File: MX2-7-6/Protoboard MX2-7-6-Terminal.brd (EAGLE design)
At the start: 54.4 x 59.2 mm, 293 parts

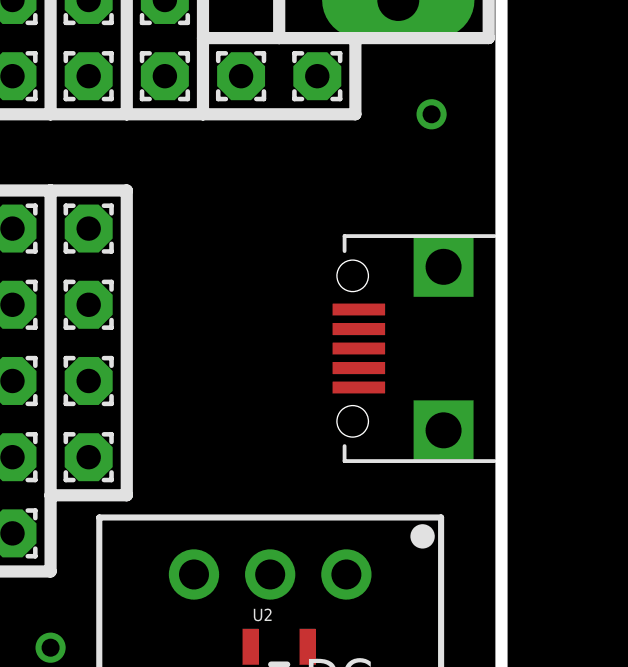
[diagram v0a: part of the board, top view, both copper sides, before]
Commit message: Change usb connector
Change to correct usb connecter and moved esp8266 bit more onto the
board.
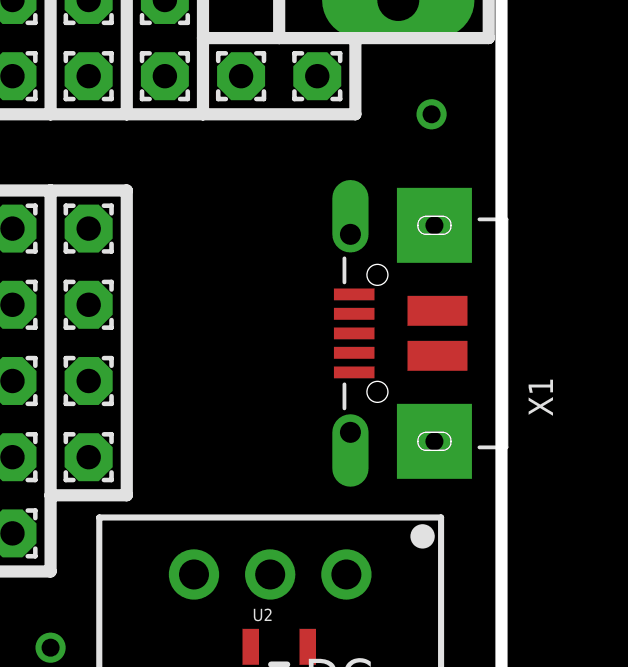
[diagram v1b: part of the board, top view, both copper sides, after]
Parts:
- removed JP1: USB-RECEPTABLE, daspilker:FCI-10103594-0001LF
- added X1: (no value), microbuilder:4UCONN_20329
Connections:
- net GND: now also X1.BASE@1, X1.BASE@2, X1.GND, X1.SPRT@1, X1.SPRT@2, X1.SPRT@3, X1.SPRT@4; no longer JP1.5
- net VCC: now also X1.VBUS; no longer JP1.1
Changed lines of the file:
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@@
 <attribute name="VALUE" x="33.02" y="55.21" size="0.0254" layer="27"/>
 </element>
-<element name="JP1" library="daspilker" package="FCI-10103594-0001LF" value="USB-RECEPTABLE" x="54.17" y="23.94" smashed="yes" rot="R90"/>
 <element name="U2" library="SparkFun-PowerIC" package="SOT23-5" value="" x="46.99" y="12.7">
 <attribute name="PROD_ID" value="VREG-00822" x="46.99" y="12.7" size="1.778" layer="27" display="off"/>
@@
 <attribute name="VALUE" x="44.45" y="40.005" size="1.27" layer="27"/>
 </element>
+<element name="X1" library="microbuilder" package="4UCONN_20329" value="" x="50.265" y="24.4475" rot="R90"/>
 </elements>
 <signals>
@@
 <contactref element="PAD33" pad="1"/>
 <contactref element="PAD36" pad="1"/>
-<contactref element="JP1" pad="5"/>
 <contactref element="U2" pad="2"/>
-<wire x1="40.64" y1="54.61" x2="43.18" y2="54.61" width="0" layer="19" extent="1-1"/>
-<wire x1="38.1" y1="54.61" x2="40.64" y2="54.61" width="0" layer="19" extent="1-1"/>
-<wire x1="35.56" y1="54.61" x2="38.1" y2="54.61" width="0" layer="19" extent="1-1"/>
-<wire x1="33.02" y1="54.61" x2="35.56" y2="54.61" width="0" layer="19" extent="1-1"/>
-<wire x1="30.48" y1="54.61" x2="33.02" y2="54.61" width="0" layer="19" extent="1-1"/>
-<wire x1="27.94" y1="54.61" x2="30.48" y2="54.61" width="0" layer="19" extent="1-1"/>
-<wire x1="25.4" y1="54.61" x2="27.94" y2="54.61" width="0" layer="19" extent="1-1"/>
-<wire x1="22.86" y1="54.61" x2="25.4" y2="54.61" width="0" layer="19" extent="1-1"/>
-<wire x1="20.32" y1="54.61" x2="22.86" y2="54.61" width="0" layer="19" extent="1-1"/>
-<wire x1="17.78" y1="54.61" x2="20.32" y2="54.61" width="0" layer="19" extent="1-1"/>
-<wire x1="15.24" y1="54.61" x2="17.78" y2="54.61" width="0" layer="19" extent="1-1"/>
-<wire x1="12.7" y1="54.61" x2="15.24" y2="54.61" width="0" layer="19" extent="1-1"/>
-<wire x1="10.16" y1="54.61" x2="12.7" y2="54.61" width="0" layer="19" extent="1-1"/>
-<wire x1="7.62" y1="54.61" x2="10.16" y2="54.61" width="0" layer="19" extent="1-1"/>
-<wire x1="5.08" y1="54.61" x2="7.62" y2="54.61" width="0" layer="19" extent="1-1"/>
-<wire x1="49.645" y1="25.24" x2="43.18" y2="54.61" width="0" layer="19" extent="1-1"/>
-<wire x1="46.69" y1="16.41" x2="49.645" y2="25.24" width="0" layer="19" extent="1-1"/>
-<wire x1="46.99" y1="11.3999" x2="46.69" y2="16.41" width="0" layer="19" extent="1-1"/>
-<wire x1="48.26" y1="5.08" x2="46.99" y2="11.3999" width="0" layer="19" extent="1-1"/>
-<wire x1="50.8" y1="5.08" x2="48.26" y2="5.08" width="0" layer="19" extent="1-1"/>
-<wire x1="45.72" y1="5.08" x2="48.26" y2="5.08" width="0" layer="19" extent="1-1"/>
-<wire x1="43.18" y1="5.08" x2="45.72" y2="5.08" width="0" layer="19" extent="1-1"/>
-<wire x1="40.64" y1="5.08" x2="43.18" y2="5.08" width="0" layer="19" extent="1-1"/>
-<wire x1="38.1" y1="5.08" x2="40.64" y2="5.08" width="0" layer="19" extent="1-1"/>
-<wire x1="35.56" y1="5.08" x2="38.1" y2="5.08" width="0" layer="19" extent="1-1"/>
-<wire x1="33.02" y1="5.08" x2="35.56" y2="5.08" width="0" layer="19" extent="1-1"/>
-<wire x1="30.48" y1="5.08" x2="33.02" y2="5.08" width="0" layer="19" extent="1-1"/>
-<wire x1="27.94" y1="5.08" x2="30.48" y2="5.08" width="0" layer="19" extent="1-1"/>
-<wire x1="25.4" y1="5.08" x2="27.94" y2="5.08" width="0" layer="19" extent="1-1"/>
-<wire x1="22.86" y1="5.08" x2="25.4" y2="5.08" width="0" layer="19" extent="1-1"/>
-<wire x1="20.32" y1="5.08" x2="22.86" y2="5.08" width="0" layer="19" extent="1-1"/>
-<wire x1="17.78" y1="5.08" x2="20.32" y2="5.08" width="0" layer="19" extent="1-1"/>
-<wire x1="15.24" y1="5.08" x2="17.78" y2="5.08" width="0" layer="19" extent="1-1"/>
-<wire x1="12.7" y1="5.08" x2="15.24" y2="5.08" width="0" layer="19" extent="1-1"/>
-<wire x1="10.16" y1="5.08" x2="12.7" y2="5.08" width="0" layer="19" extent="1-1"/>
-<wire x1="7.62" y1="5.08" x2="10.16" y2="5.08" width="0" layer="19" extent="1-1"/>
-<wire x1="5.08" y1="5.08" x2="7.62" y2="5.08" width="0" layer="19" extent="1-1"/>
+<contactref element="X1" pad="SPRT@4"/>
+<contactref element="X1" pad="BASE@2"/>
+<contactref element="X1" pad="SPRT@3"/>
+<contactref element="X1" pad="GND"/>
+<contactref element="X1" pad="SPRT@2"/>
+<contactref element="X1" pad="BASE@1"/>
+<contactref element="X1" pad="SPRT@1"/>
 </signal>
 <signal name="VCC">
 <contactref element="DC" pad="1"/>
-<contactref element="JP1" pad="1"/>
 <contactref element="U2" pad="3"/>
 <contactref element="U2" pad="1"/>
-<wire x1="49.23" y1="16.41" x2="49.645" y2="22.64" width="0" layer="19" extent="1-1"/>
+<contactref element="X1" pad="VBUS"/>
+<wire x1="49.23" y1="16.41" x2="49.49" y2="23.1475" width="0" layer="19" extent="1-1"/>
 <wire x1="47.94" y1="11.3999" x2="49.23" y2="16.41" width="0" layer="19" extent="1-1"/>
 <wire x1="46.04" y1="11.3999" x2="47.94" y2="11.3999" width="0" layer="19" extent="1-1"/>
@@
 <contactref element="JP6" pad="1"/>
 <contactref element="JP2" pad="P$1"/>
-<wire x1="50.96" y1="50.8" x2="45.72" y2="48.26" width="0" layer="19" extent="1-1"/>
+<wire x1="45.72" y1="48.26" x2="50.96" y2="50.8" width="0" layer="19" extent="1-1"/>
 </signal>
 <signal name="N$4">
 <contactref element="JP3" pad="P$1"/>
 <contactref element="JP7" pad="1"/>
-<wire x1="50.96" y1="43.18" x2="45.72" y2="45.72" width="0" layer="19" extent="1-1"/>
+<wire x1="45.72" y1="45.72" x2="50.96" y2="43.18" width="0" layer="19" extent="1-1"/>
 </signal>
 <signal name="N$5">

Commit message: Update esp component and usb
test
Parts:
- removed JP4: (no value), adafruit:1X1-BIGPOGO
- removed JP6, JP7, JP8: (no value), adafruit:1X01-CLEANBIG
- removed PAD1, PAD100, PAD101, PAD102, PAD103, PAD106, PAD107, PAD108, PAD109, PAD110, PAD111, PAD112, PAD115, PAD116, PAD117, PAD118, PAD119, PAD120, PAD121, PAD124, PAD125, PAD126, PAD127, PAD128, PAD129, PAD130, PAD133, PAD134, PAD135, PAD136, PAD137, PAD138, PAD139, PAD142, PAD143, PAD144, PAD145, PAD146, PAD147, PAD148, PAD151, PAD152, PAD153, PAD154, PAD155, PAD156, PAD157, PAD160, PAD161, PAD162, PAD163, PAD164, PAD165, PAD166, PAD169, PAD170, PAD171, PAD172, PAD173, PAD174, PAD175, PAD178, PAD179, PAD180, PAD181, PAD182, PAD183, PAD184, PAD187, PAD188, PAD189, PAD190, PAD191, PAD192, PAD193, PAD196, PAD197, PAD198, PAD199, PAD2, PAD200, PAD201, PAD202, PAD205, PAD206, PAD207, PAD208, PAD209, PAD210, PAD211, PAD214, PAD215, PAD216, PAD217, PAD218, PAD219, PAD220, PAD260, PAD261, PAD262, PAD263, PAD264, PAD265, PAD266, PAD269, PAD270, PAD271, PAD272, PAD273, PAD274, PAD275, PAD278, PAD279, PAD280, PAD281, PAD282, PAD283, PAD284, PAD287, PAD288, PAD289, PAD290, PAD291, PAD292, PAD293, PAD296, PAD297, PAD298, PAD299, PAD300, PAD301, PAD302, PAD305, PAD306, PAD307, PAD308, PAD309, PAD310, PAD311, PAD314, PAD315, PAD316, PAD317, PAD318, PAD319, PAD320, PAD332, PAD333, PAD334, PAD335, PAD336, PAD337, PAD338, PAD341, PAD342, PAD343, PAD344, PAD345, PAD346, PAD347, PAD350, PAD351, PAD352, PAD353, PAD354, PAD355, PAD356, PAD359, PAD360, PAD361, PAD362, PAD363, PAD364, PAD365, PAD368, PAD369, PAD370, PAD371, PAD372, PAD373, PAD374, PAD377, PAD378, PAD379, PAD380, PAD381, PAD382, PAD383, PAD385, PAD386, PAD387, PAD388, PAD389, PAD391, PAD392, PAD393, PAD394, PAD79, PAD80, PAD81, PAD82, PAD83, PAD84, PAD85, PAD88, PAD89, PAD90, PAD91, PAD92, PAD93, PAD94, PAD97, PAD98, PAD99: (no value), wirepad:1,6/0,8
- added J10, J11, J12, J13, J14, J15, J16, J17, J18, J19, J2, J20, J21, J22, J23, J24, J25, J26, J27, J28, J29, J3, J30, J4, J5, J6, J7, J8, J9: (no value), SparkFun-Connectors:1X07_NO_SILK
- added J31: (no value), SparkFun-Connectors:1X05_NO_SILK
- added J32: (no value), SparkFun-Connectors:1X03_NO_SILK
- added J36, J37, J38: (no value), SparkFun-Connectors:1X01_NO_SILK
- added JP1: (no value), adafruit:1X1-BIGPOGO
- moved JP2 9.53 mm to (51.0, 41.3)
- moved JP3 3.18 mm to (51.0, 46.4)
- moved X1 2.22 mm to (50.3, 26.7)
- moved U2 0.64 mm to (46.4, 12.7), turned to 180 degrees
- moved DC 0.64 mm to (46.7, 17.0)
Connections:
- removed net N$40: PAD377.1, PAD378.1, PAD379.1, PAD380.1, PAD381.1, PAD382.1, PAD383.1
- removed net N$41: PAD385.1, PAD386.1, PAD387.1, PAD388.1, PAD389.1
- new net N$6: J4.1, J4.2, J4.3, J4.4, J4.5, J4.6, J4.7
- net N$1: now also J2.1, J2.2, J2.3, J2.4, J2.5, J2.6, J2.7; no longer PAD391.1, PAD392.1, PAD393.1, PAD394.1
- net N$10: now also J8.1, J8.2, J8.3, J8.4, J8.5, J8.6, J8.7; no longer PAD106.1, PAD107.1, PAD108.1, PAD109.1, PAD110.1, PAD111.1, PAD112.1
- net N$11: now also J9.1, J9.2, J9.3, J9.4, J9.5, J9.6, J9.7; no longer PAD115.1, PAD116.1, PAD117.1, PAD118.1, PAD119.1, PAD120.1, PAD121.1
- net N$12: now also J10.1, J10.2, J10.3, J10.4, J10.5, J10.6, J10.7; no longer PAD124.1, PAD125.1, PAD126.1, PAD127.1, PAD128.1, PAD129.1, PAD130.1
- net N$13: now also J11.1, J11.2, J11.3, J11.4, J11.5, J11.6, J11.7; no longer PAD133.1, PAD134.1, PAD135.1, PAD136.1, PAD137.1, PAD138.1, PAD139.1
- net N$14: now also J12.1, J12.2, J12.3, J12.4, J12.5, J12.6, J12.7; no longer PAD142.1, PAD143.1, PAD144.1, PAD145.1, PAD146.1, PAD147.1, PAD148.1
- net N$15: now also J13.1, J13.2, J13.3, J13.4, J13.5, J13.6, J13.7; no longer PAD151.1, PAD152.1, PAD153.1, PAD154.1, PAD155.1, PAD156.1, PAD157.1
- net N$16: now also J14.1, J14.2, J14.3, J14.4, J14.5, J14.6, J14.7; no longer PAD160.1, PAD161.1, PAD162.1, PAD163.1, PAD164.1, PAD165.1, PAD166.1
- net N$17: now also J15.1, J15.2, J15.3, J15.4, J15.5, J15.6, J15.7; no longer PAD169.1, PAD170.1, PAD171.1, PAD172.1, PAD173.1, PAD174.1, PAD175.1
- net N$18: now also J16.1, J16.2, J16.3, J16.4, J16.5, J16.6, J16.7; no longer PAD178.1, PAD179.1, PAD180.1, PAD181.1, PAD182.1, PAD183.1, PAD184.1
- net N$19: now also J17.1, J17.2, J17.3, J17.4, J17.5, J17.6, J17.7; no longer PAD187.1, PAD188.1, PAD189.1, PAD190.1, PAD191.1, PAD192.1, PAD193.1
- net N$2: now also J36.1, JP3.P$1; no longer JP2.P$1, JP6.1
- net N$20: now also J18.1, J18.2, J18.3, J18.4, J18.5, J18.6, J18.7; no longer PAD196.1, PAD197.1, PAD198.1, PAD199.1, PAD200.1, PAD201.1, PAD202.1
- net N$21: now also J19.1, J19.2, J19.3, J19.4, J19.5, J19.6, J19.7; no longer PAD205.1, PAD206.1, PAD207.1, PAD208.1, PAD209.1, PAD210.1, PAD211.1
- net N$22: now also J20.1, J20.2, J20.3, J20.4, J20.5, J20.6, J20.7; no longer PAD214.1, PAD215.1, PAD216.1, PAD217.1, PAD218.1, PAD219.1, PAD220.1
- net N$27: now also J21.1, J21.2, J21.3, J21.4, J21.5, J21.6, J21.7; no longer PAD260.1, PAD261.1, PAD262.1, PAD263.1, PAD264.1, PAD265.1, PAD266.1
- net N$28: now also J22.1, J22.2, J22.3, J22.4, J22.5, J22.6, J22.7; no longer PAD269.1, PAD270.1, PAD271.1, PAD272.1, PAD273.1, PAD274.1, PAD275.1
- net N$29: now also J23.1, J23.2, J23.3, J23.4, J23.5, J23.6, J23.7; no longer PAD278.1, PAD279.1, PAD280.1, PAD281.1, PAD282.1, PAD283.1, PAD284.1
- net N$3: now also J37.1, JP2.P$1; no longer PAD1.1, PAD2.1
- net N$30: now also J24.1, J24.2, J24.3, J24.4, J24.5, J24.6, J24.7; no longer PAD287.1, PAD288.1, PAD289.1, PAD290.1, PAD291.1, PAD292.1, PAD293.1
- net N$31: now also J25.1, J25.2, J25.3, J25.4, J25.5, J25.6, J25.7; no longer PAD296.1, PAD297.1, PAD298.1, PAD299.1, PAD300.1, PAD301.1, PAD302.1
- net N$32: now also J26.1, J26.2, J26.3, J26.4, J26.5, J26.6, J26.7; no longer PAD305.1, PAD306.1, PAD307.1, PAD308.1, PAD309.1, PAD310.1, PAD311.1
- net N$33: now also J27.1, J27.2, J27.3, J27.4, J27.5, J27.6, J27.7; no longer PAD314.1, PAD315.1, PAD316.1, PAD317.1, PAD318.1, PAD319.1, PAD320.1
- net N$35: now also J28.1, J28.2, J28.3, J28.4, J28.5, J28.6, J28.7; no longer PAD332.1, PAD333.1, PAD334.1, PAD335.1, PAD336.1, PAD337.1, PAD338.1
- net N$36: now also J29.1, J29.2, J29.3, J29.4, J29.5, J29.6, J29.7; no longer PAD341.1, PAD342.1, PAD343.1, PAD344.1, PAD345.1, PAD346.1, PAD347.1
- net N$37: now also J30.1, J30.2, J30.3, J30.4, J30.5, J30.6, J30.7; no longer PAD350.1, PAD351.1, PAD352.1, PAD353.1, PAD354.1, PAD355.1, PAD356.1
- net N$38: now also J31.1, J31.2, J31.3, J31.4, J31.5; no longer PAD359.1, PAD360.1, PAD361.1, PAD362.1, PAD363.1, PAD364.1, PAD365.1
- net N$39: now also J32.1, J32.2, J32.3; no longer PAD368.1, PAD369.1, PAD370.1, PAD371.1, PAD372.1, PAD373.1, PAD374.1
- net N$4: now also J38.1, JP1.P$1; no longer JP3.P$1, JP7.1
- net N$5: now also J3.1, J3.2, J3.3, J3.4, J3.5, J3.6, J3.7; no longer JP4.P$1, JP8.1
- net N$7: now also J5.1, J5.2, J5.3, J5.4, J5.5, J5.6, J5.7; no longer PAD79.1, PAD80.1, PAD81.1, PAD82.1, PAD83.1, PAD84.1, PAD85.1
- net N$8: now also J6.1, J6.2, J6.3, J6.4, J6.5, J6.6, J6.7; no longer PAD88.1, PAD89.1, PAD90.1, PAD91.1, PAD92.1, PAD93.1, PAD94.1
- net N$9: now also J7.1, J7.2, J7.3, J7.4, J7.5, J7.6, J7.7; no longer PAD100.1, PAD101.1, PAD102.1, PAD103.1, PAD97.1, PAD98.1, PAD99.1
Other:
- board text added: "3.3V"
- board text removed: "VDD"
